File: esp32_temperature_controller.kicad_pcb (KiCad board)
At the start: 2 copper layers, 40 x 97.9 mm, 40 parts, among them J1 ESP32-DevKitC J1, J2 ESP32-DevKitC J2, J3 AC 220V, J4 Heater, J5 RTD1, J6 RTD2, J7 DHT20, U1 MAX31865xTP, U2 MAX31865xTP, U3 EL817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

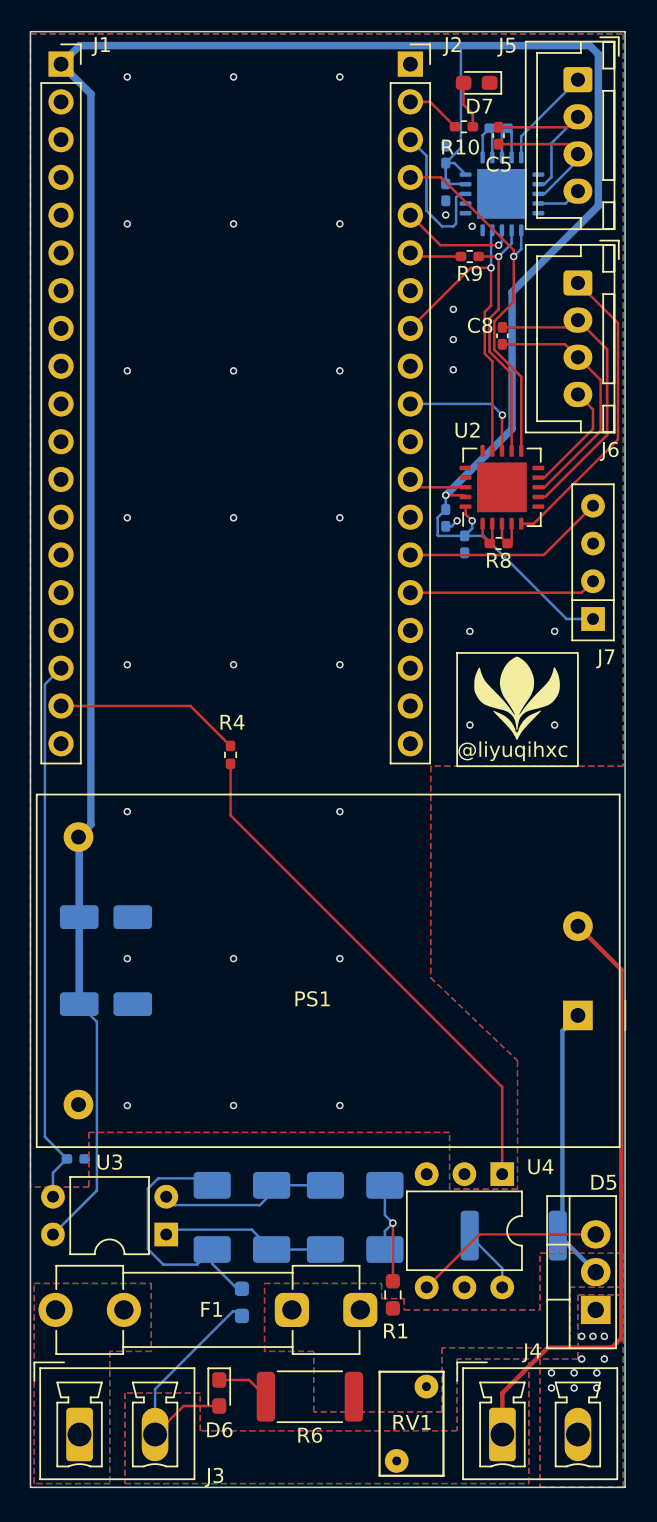
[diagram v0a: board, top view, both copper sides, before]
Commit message: add debug port; change max31865 to ssop-20
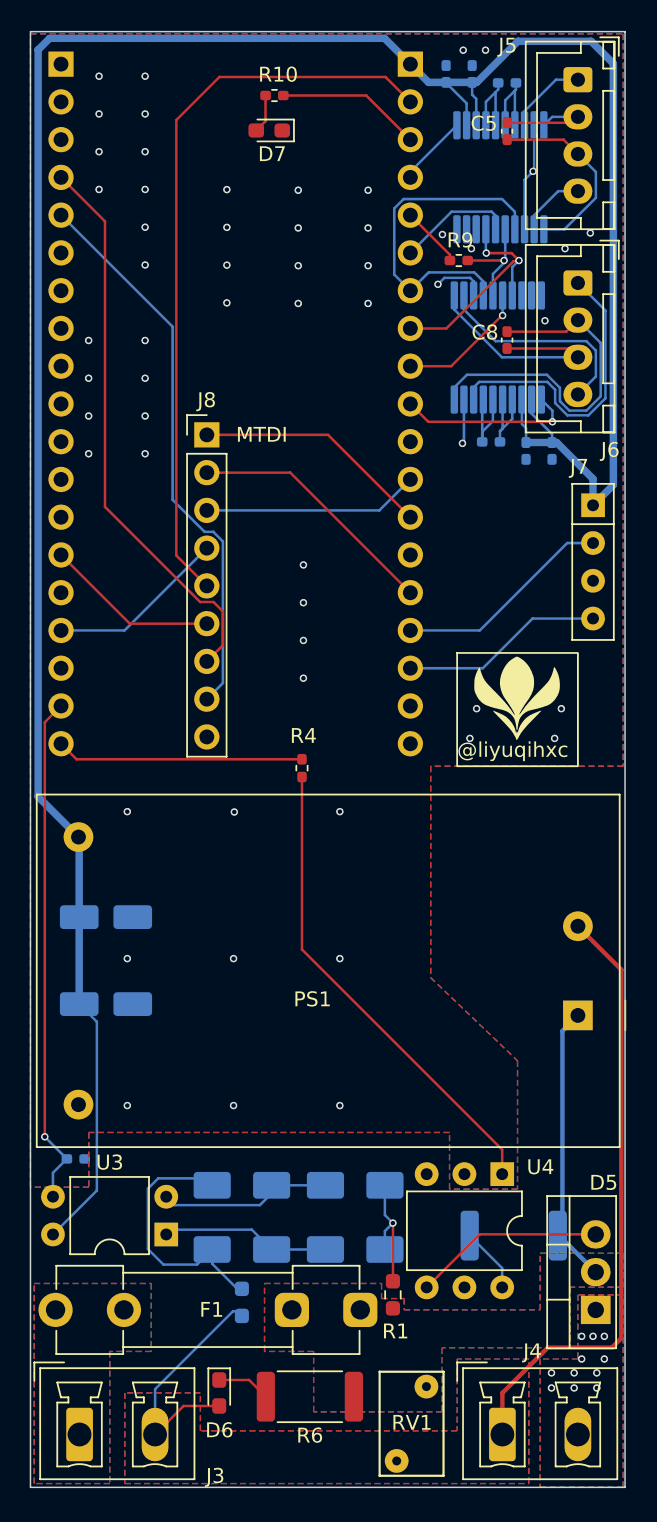
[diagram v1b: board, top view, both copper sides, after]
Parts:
- added J8: JTAG, Connector_PinHeader_2.54mm:PinHeader_1x09_P2.54mm_Vertical, F.Cu at (96.7, 64.8)
- J1, J2, R8: moved to B.Cu
- U1: value MAX31865xTP -> MAX31865xAP; footprint Package_DFN_QFN:QFN-20-1EP_5x5mm_P0.65mm_EP3.35x3.35mm -> Package_SO:SSOP-20_5.3x7.2mm_P0.65mm
- U2: value MAX31865xTP -> MAX31865xAP; footprint Package_DFN_QFN:QFN-20-1EP_5x5mm_P0.65mm_EP3.35x3.35mm -> Package_SO:SSOP-20_5.3x7.2mm_P0.65mm; moved to B.Cu
- moved J1 23.5 mm to (110.4, 39.9), turned to 180 degrees
- moved J2 23.5 mm to (86.9, 39.9), turned to 180 degrees
- moved D7 14.3 mm to (100.9, 44.4)
- moved R10 12.9 mm to (101.2, 42.0), turned to 180 degrees
- moved U2 9.41 mm to (116.3, 59.0)
- moved C7 8.45 mm to (119.9, 65.9)
- moved C4 7.96 mm to (112.8, 40.5), turned to -90 degrees
- moved J7 7.65 mm to (122.7, 69.6), turned to -90 degrees
- moved C6 7.52 mm to (118.2, 65.9)
- moved R8 6.85 mm to (115.8, 65.3), turned to 0 degrees
- moved C3 5.71 mm to (114.5, 40.5)
- moved R4 4.88 mm to (103.1, 87.2)
- moved R7 3.10 mm to (116.9, 41.1)
- moved U1 1.12 mm to (116.5, 47.5)
- moved R9 0.78 mm to (113.7, 53.1)
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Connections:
- J1 pad 10: unconnected-(J1-Pin_10-Pad10) -> /TEMP2_RDY
- J1 pad 12: unconnected-(J1-Pin_12-Pad12) -> /MTMS
- J1 pad 13: unconnected-(J1-Pin_13-Pad13) -> /MTDI
- J1 pad 15: unconnected-(J1-Pin_15-Pad15) -> /MTCK
- J1 pad 16: unconnected-(J1-Pin_16-Pad16) -> /DHT_SDA
- J1 pad 17: /ZERO_CROSS -> /DHT_SCL
- J1 pad 18: /HEATER_CTRL -> unconnected-(J1-Pin_18-Pad18)
- J1 pad 2: unconnected-(J1-Pin_2-Pad2) -> /EN
- J1 pad 3: unconnected-(J1-Pin_3-Pad3) -> /LED_HEATER
- J1 pad 4: unconnected-(J1-Pin_4-Pad4) -> /TEMP1_RDY
- J1 pad 5: unconnected-(J1-Pin_5-Pad5) -> Net-(J1-Pin_5)
- J1 pad 6: unconnected-(J1-Pin_6-Pad6) -> /TEMP1_CS
- J1 pad 7: unconnected-(J1-Pin_7-Pad7) -> /TEMP_DI
- J1 pad 8: unconnected-(J1-Pin_8-Pad8) -> /TEMP_DO
- J1 pad 9: unconnected-(J1-Pin_9-Pad9) -> /TEMP2_CS
- J2 pad 10: /TEMP2_CS -> unconnected-(J2-Pin_10-Pad10)
- J2 pad 12: /TEMP2_RDY -> unconnected-(J2-Pin_12-Pad12)
- J2 pad 14: /DHT_SCL -> /BOOT
- J2 pad 15: /DHT_SDA -> unconnected-(J2-Pin_15-Pad15)
- J2 pad 16: unconnected-(J2-Pin_16-Pad16) -> /MTDO
- J2 pad 18: unconnected-(J2-Pin_18-Pad18) -> /ZERO_CROSS
- J2 pad 19: unconnected-(J2-Pin_19-Pad19) -> /HEATER_CTRL
- J2 pad 2: /LED_HEATING_STATE -> unconnected-(J2-Pin_2-Pad2)
- J2 pad 3: /TEMP1_RDY -> unconnected-(J2-Pin_3-Pad3)
- J2 pad 4: /TEMP_DI -> /TX0
- J2 pad 5: /TEMP1_CS -> /RX0
- J2 pad 6: Net-(J2-Pin_6) -> unconnected-(J2-Pin_6-Pad6)
- J2 pad 8: /TEMP_DO -> unconnected-(J2-Pin_8-Pad8)
- R10 pad 1: /LED_HEATING_STATE -> /LED_HEATER
- R9 pad 2: Net-(J2-Pin_6) -> Net-(J1-Pin_5)
- U1 pad 1: Net-(U1-BIAS) -> /TEMP1_RDY
- U1 pad 10: GND -> Net-(J5-Pin_2)
- U1 pad 11: /TEMP_DI -> Net-(J5-Pin_3)
- U1 pad 12: /TEMP_CLK -> Net-(J5-Pin_4)
- U1 pad 13: /TEMP1_CS -> GND
- U1 pad 14: /TEMP_DO -> /TEMP_DI
- U1 pad 15: GND -> /TEMP_CLK
- U1 pad 16: GND -> /TEMP1_CS
- U1 pad 17: unconnected-(U1-NC-Pad17) -> /TEMP_DO
- U1 pad 18: /TEMP1_RDY -> GND
- U1 pad 19: +3V3 -> GND
- U1 pad 2: Net-(U1-BIAS) -> +3V3
- U1 pad 20: +3V3 -> unconnected-(U1-NC-Pad20)
- U1 pad 3: Net-(U1-ISENSOR) -> +3V3
- U1 pad 4: Net-(U1-ISENSOR) -> Net-(U1-BIAS)
- U1 pad 5: Net-(J5-Pin_1) -> Net-(U1-BIAS)
- U1 pad 6: GND -> Net-(U1-ISENSOR)
- U1 pad 7: Net-(J5-Pin_2) -> Net-(U1-ISENSOR)
- U1 pad 8: Net-(J5-Pin_3) -> Net-(J5-Pin_1)
- U1 pad 9: Net-(J5-Pin_4) -> GND
- U2 pad 1: Net-(U2-BIAS) -> /TEMP2_RDY
- U2 pad 10: GND -> Net-(J6-Pin_2)
- U2 pad 11: /TEMP_DI -> Net-(J6-Pin_3)
- U2 pad 12: /TEMP_CLK -> Net-(J6-Pin_4)
- U2 pad 13: /TEMP2_CS -> GND
- U2 pad 14: /TEMP_DO -> /TEMP_DI
- U2 pad 15: GND -> /TEMP_CLK
- U2 pad 16: GND -> /TEMP2_CS
- U2 pad 17: unconnected-(U2-NC-Pad17) -> /TEMP_DO
- U2 pad 18: /TEMP2_RDY -> GND
- U2 pad 19: +3V3 -> GND
- U2 pad 2: Net-(U2-BIAS) -> +3V3
- U2 pad 20: +3V3 -> unconnected-(U2-NC-Pad20)
- U2 pad 3: Net-(U2-ISENSOR) -> +3V3
- U2 pad 4: Net-(U2-ISENSOR) -> Net-(U2-BIAS)
- U2 pad 5: Net-(J6-Pin_1) -> Net-(U2-BIAS)
- U2 pad 6: GND -> Net-(U2-ISENSOR)
- U2 pad 7: Net-(J6-Pin_2) -> Net-(U2-ISENSOR)
- U2 pad 8: Net-(J6-Pin_3) -> Net-(J6-Pin_1)
- U2 pad 9: Net-(J6-Pin_4) -> GND
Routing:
- net /EN: track 0.00 -> 49.8 mm
- net /TX0: track 0.00 -> 38.0 mm
- net /RX0: track 0.00 -> 37.9 mm
- net /MTCK: track 0.00 -> 17.0 mm
- net /MTDI: track 0.00 -> 16.0 mm
- net /MTMS: track 0.00 -> 14.6 mm
- net GND: track 0.92 -> 13.9 mm, vias 33 -> 57
- net /MTDO: track 0.00 -> 12.1 mm
- net /BOOT: track 0.00 -> 11.7 mm
- net /TEMP_CLK: track 17.4 -> 7.24 mm
- net /LED_HEATER: track 0.00 -> 9.77 mm
- net +3V3: track 184.8 -> 175.1 mm, vias 2 -> 0
- net /TEMP2_RDY: track 3.94 -> 11.9 mm, vias 0 -> 1
- net Net-(J6-Pin_4): track 7.79 -> 14.4 mm
- net /TEMP_DO: track 22.4 -> 15.8 mm, vias 1 -> 2
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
